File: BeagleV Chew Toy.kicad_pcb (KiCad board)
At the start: 2 copper layers, 69.2 x 51.7 mm, 147 parts, among them J1 Conn_02x05_Counter_Clockwise, J2 Conn_02x05_Counter_Clockwise, J3 Conn_02x05_Counter_Clockwise, U1 74HC245, U2 74HC245, U3 74HC245, U4 74HC245

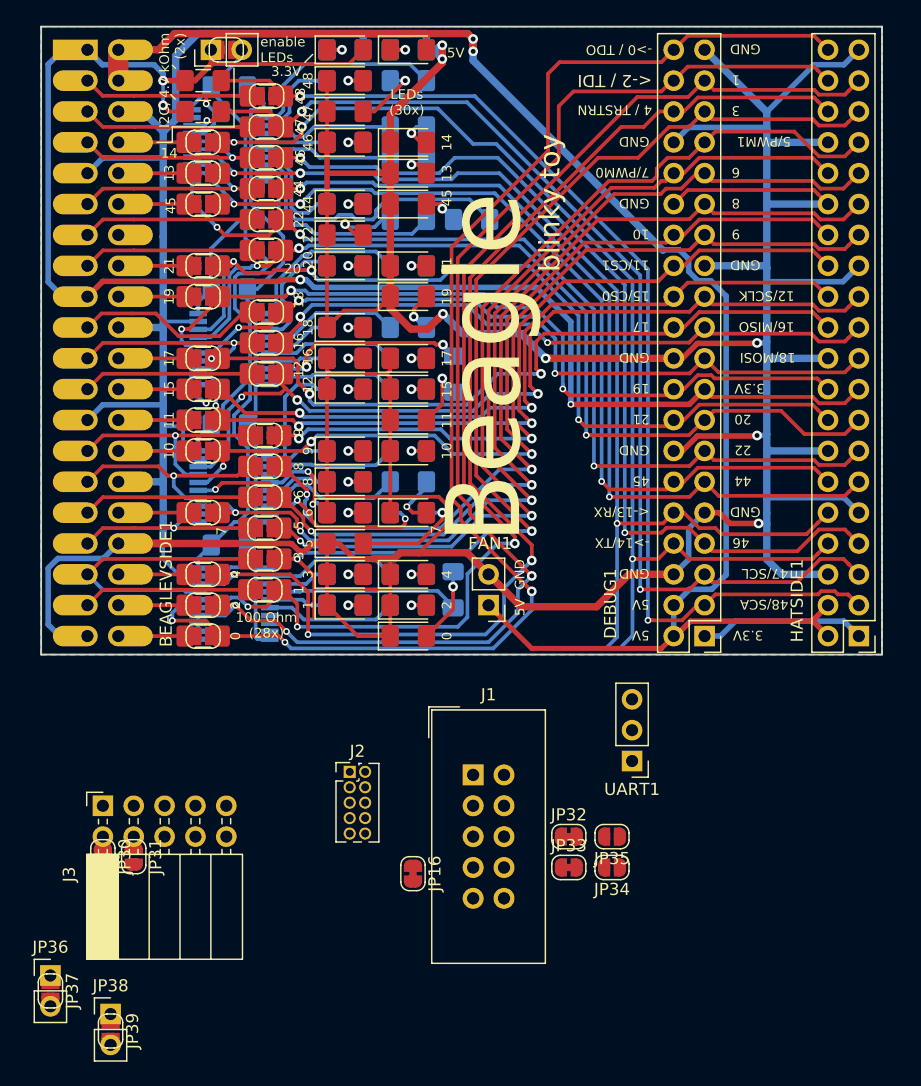
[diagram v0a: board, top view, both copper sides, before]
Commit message: small silk improvements
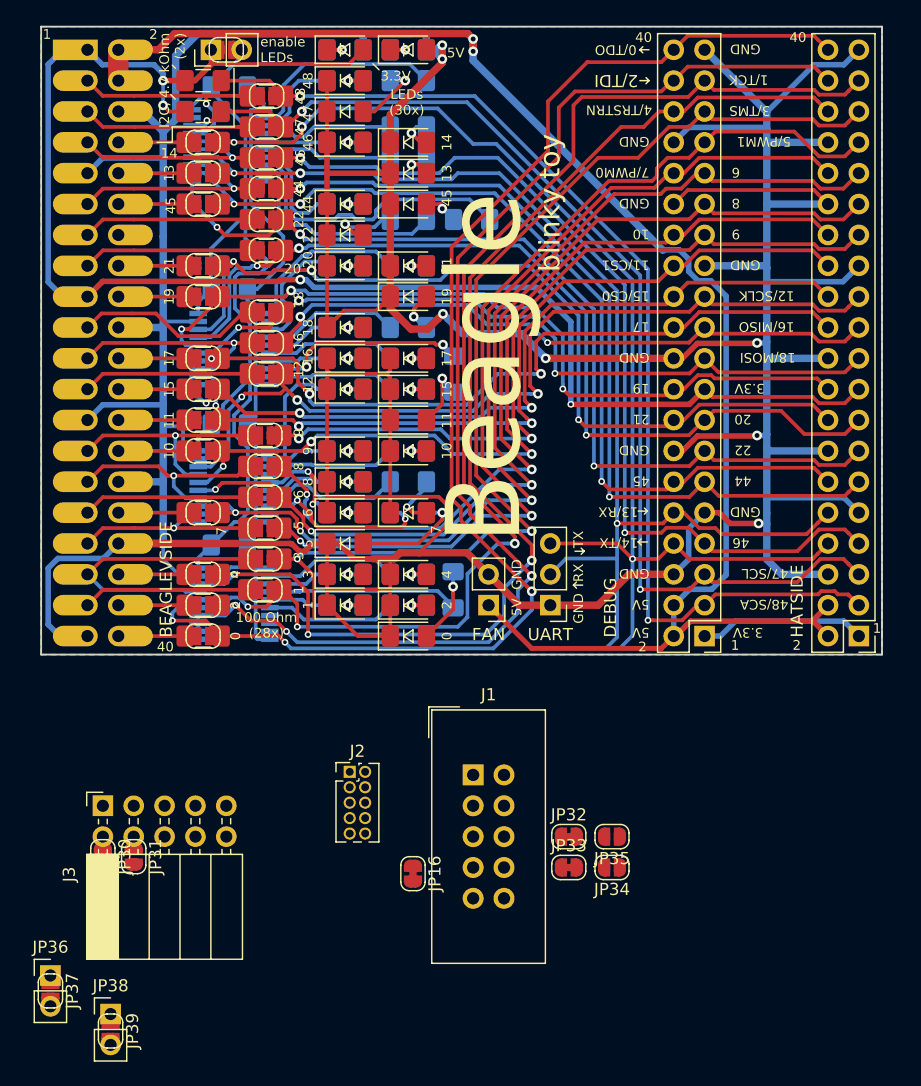
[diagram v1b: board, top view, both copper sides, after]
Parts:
- C1, C2, C3, C4: value 100n -> 100nF
- moved UART1 14.5 mm to (167.8, 126.5)
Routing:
- net /GPIO14/TX: track 94.0 -> 101.2 mm
- net /GPIO13/RX: track 90.9 -> 96.9 mm
- net /GPIO1_TCK: track 99.2 -> 101.9 mm
- net /GPIO0_TDO_FROM_SOC: track 110.9 -> 109.5 mm
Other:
- board text added: "0/TDO"
- board text added: "1/TCK"
- board text added: "13/RX"
- board text added: "14/TX"
- board text added: "2/TDI"
- board text added: "3/TMS"
- board text added: "4/TRSTRN"
- board text added: "40"
- board text added: "BEAGLEVSIDE"
- board text added: "DEBUG"
- board text added: "FAN"
- board text added: "HATSIDE"
- board text added: "RX"
- board text added: "TX"
- board text added: "UART"
- board text removed: "- connect UART - make 5V, 3V3, GND wider - add silk for LEDs"
- board text removed: "->0 / TDO"
- board text removed: "->14/TX"
- board text removed: "4 / TRSTRN"
- board text removed: "<-13/RX"
- board text removed: "<-2 / TDI"

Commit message: mostly done
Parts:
- added G***: LOGO, BeagleV Chew Toy:subraum_5mm, B.Cu at (165.5, 83.4)
- added G***: LOGO, BeagleV Chew Toy:subraum_5mm, F.Cu at (169.2, 116.6)
- added G***: LOGO, BeagleV Chew Toy:subraum_5mm, F.Cu at (190.4, 136.1)
- added G***: LOGO, BeagleV Chew Toy:subraum_10mm, B.Cu at (189.2, 134.9)
- JP32, JP33, JP34, JP35: moved to B.Cu
- moved JP37 60.8 mm to (183.0, 135.4), turned to 90 degrees
- moved JP36 59.9 mm to (183.0, 136.7), turned to 180 degrees
- moved JP39 53.2 mm to (177.9, 135.4), turned to 90 degrees
- moved JP38 52.0 mm to (177.9, 136.7), turned to 180 degrees
- moved JP31 43.1 mm to (173.2, 130.6), turned to 90 degrees
- moved JP30 42.7 mm to (170.3, 130.6), turned to 90 degrees
- moved JP34 33.2 mm to (144.0, 131.7), turned to 90 degrees
- moved J3 33.0 mm to (162.7, 134.1)
- moved JP33 32.4 mm to (141.4, 131.7), turned to 90 degrees
- moved J1 29.6 mm to (132.1, 136.7), turned to 90 degrees
- moved JP35 27.3 mm to (149.4, 131.7), turned to 90 degrees
- moved JP32 26.5 mm to (146.7, 131.7), turned to 90 degrees
- moved JP16 13.6 mm to (149.0, 137.3)
- moved J2 4.33 mm to (151.5, 135.9), turned to 90 degrees
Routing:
- net +3V3: track 143.3 -> 244.5 mm, vias 4 -> 5
- net GND: track 557.4 -> 607.6 mm, vias 7 -> 9
- net /GPIO3_TMS: track 88.5 -> 131.4 mm, vias 2 -> 4
- net /GPIO4_TRSTN: track 99.1 -> 138.5 mm, vias 3 -> 4
- net /GPIO1_TCK: track 101.9 -> 136.6 mm, vias 3 -> 5
- net Net-(J1-Pad8): track 0.00 -> 22.8 mm, vias 0 -> 2
- net Net-(J1-Pad6): track 0.00 -> 20.4 mm, vias 0 -> 3
- net Net-(J1-Pad7): track 0.00 -> 17.9 mm
- net Net-(J1-Pad9): track 0.00 -> 16.7 mm
- net Net-(J3-Pad6): track 0.00 -> 16.2 mm
- net /GPIO2_TDI_TO_SOC: track 105.0 -> 118.6 mm, vias 3 -> 4
- net Net-(J3-Pad2): track 0.00 -> 12.3 mm, vias 0 -> 2
- net Net-(J3-Pad4): track 0.00 -> 11.6 mm, vias 0 -> 1
- net /GPIO14/TX: track 101.2 -> 109.9 mm
- net Net-(J3-Pad8): track 0.00 -> 8.58 mm
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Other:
- board size 69.2 x 51.7 mm -> 69.2 x 61.6 mm
- board text added: "ARM 10-pin"
- board text added: "BEAGLEV SIDE"
- board text added: "GNDDetect"
- board text added: "HAT SIDE"
- board text added: "Sipeed RV"
- board text added: "TCK"
- board text added: "TDO"
- board text added: "TMS"
- board text added: "TRST"
- board text removed: "BEAGLEVSIDE"
- board text removed: "HATSIDE"

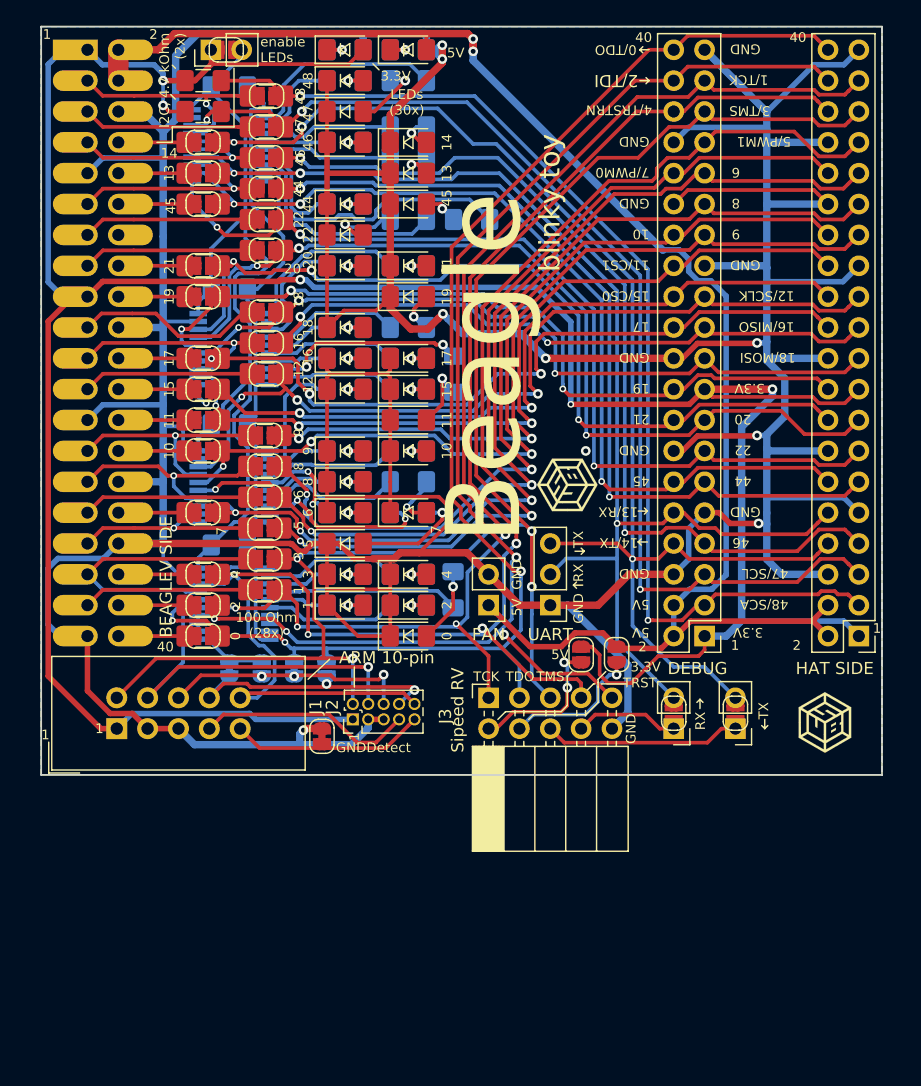
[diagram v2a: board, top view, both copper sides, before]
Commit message: rotate text in silk
Some of it was in a different orientation than the others.
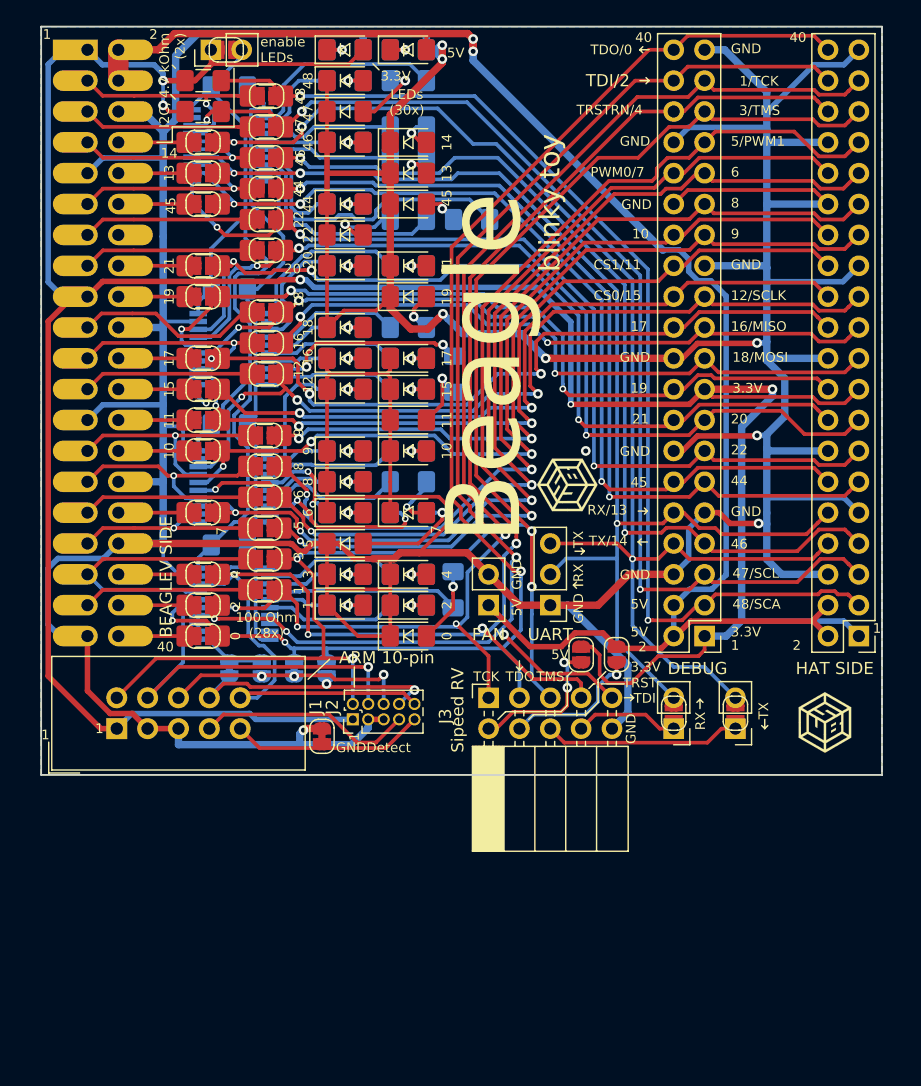
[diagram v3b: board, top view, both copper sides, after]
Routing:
- net GND: track 607.6 -> 609.4 mm
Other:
- board text added: "CS0/15"
- board text added: "CS1/11"
- board text added: "PWM0/7"
- board text added: "RX/13"
- board text added: "TDI"
- board text added: "TDI/2"
- board text added: "TDI/TDO flipped"
- board text added: "TDO/0"
- board text added: "TRSTRN/4"
- board text added: "TX/14"
- board text removed: "0/TDO"
- board text removed: "11/CS1"
- board text removed: "13/RX"
- board text removed: "14/TX"
- board text removed: "15/CS0"
- board text removed: "2/TDI"
- board text removed: "4/TRSTRN"
- board text removed: "7/PWM0"

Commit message: bugfix: lower left corner would have collided with heatsink mount
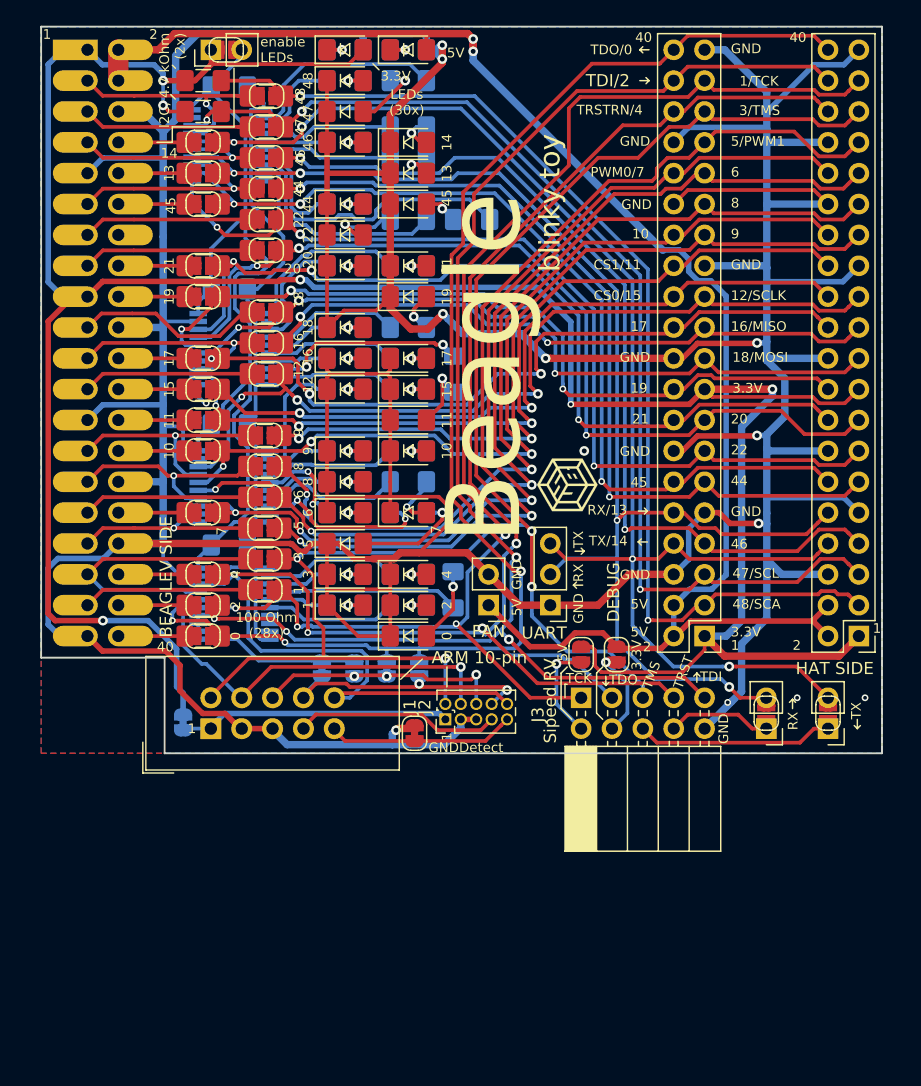
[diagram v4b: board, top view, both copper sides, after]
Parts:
- removed the G*** at (189.2, 134.9)
- added JP42: SolderJumper_2_Bridged, Jumper:SolderJumper-2_P1.3mm_Bridged_RoundedPad1.0x1.5mm, B.Cu at (137.5, 136.1)
- G***: moved to B.Cu
- moved G*** 20.4 mm to (185.7, 116.3), turned to 180 degrees
- moved J1 7.75 mm to (139.8, 136.7)
- moved JP16 7.62 mm to (156.6, 137.0)
- moved J2 7.62 mm to (159.1, 135.9)
- moved JP32 7.62 mm to (154.3, 131.7)
- moved JP33 7.62 mm to (149.0, 131.7)
- moved JP34 7.62 mm to (151.6, 131.7)
- moved JP35 7.62 mm to (157.0, 131.7)
- moved JP36 7.62 mm to (190.6, 136.7)
- moved JP37 7.62 mm to (190.6, 135.4)
- moved JP38 7.62 mm to (185.5, 136.7)
- moved JP39 7.62 mm to (185.5, 135.4)
- moved J3 7.62 mm to (170.3, 134.1)
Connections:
- J1 pad 1: +3V3 -> Net-(J1-Pad1)
- J2 pad 1: +3V3 -> Net-(J1-Pad1)
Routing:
- net Net-(J1-Pad1): track 0.00 -> 22.5 mm
- net /GPIO2_TDI_TO_SOC: track 118.6 -> 136.1 mm
- net /GPIO4_TRSTN: track 138.5 -> 153.1 mm
- net +3V3: track 244.5 -> 232.1 mm, vias 5 -> 6
- net /GPIO1_TCK: track 136.6 -> 146.0 mm
- net /GPIO0_TDO_FROM_SOC: track 113.9 -> 122.6 mm
- net /GPIO14/TX: track 109.9 -> 117.5 mm, vias 3 -> 4
- net /GPIO13/RX: track 102.5 -> 110.0 mm, vias 3 -> 4
- net GND: track 609.4 -> 616.7 mm, vias 9 -> 12
- net /GPIO3_TMS: track 131.4 -> 136.5 mm
- net Net-(J3-Pad2): track 12.3 -> 8.25 mm, vias 2 -> 1
- net Net-(J3-Pad4): track 11.6 -> 7.62 mm
- net Net-(J1-Pad9): track 16.7 -> 15.8 mm
- net Net-(J1-Pad7): track 17.9 -> 17.0 mm
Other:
- board size 69.2 x 61.6 mm -> 69.2 x 59.8 mm

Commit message: add UART1 and PWM2 to silk screen
also add the .sch file again...
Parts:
- moved G*** 3.06 mm to (169.4, 113.5)
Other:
- board text added: "I2C1"
- board text added: "PWM2/45"
- board text added: "UART1 9/RX"
- board text added: "UART1 TX/10"
- board text added: "UART3"
- board text removed: "UART"
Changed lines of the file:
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@@
   (general
     (thickness 1.6)
-    (drawings 314)
+    (drawings 322)
     (tracks 1793)
     (zones 0)
@@
   )
   (module "BeagleV Chew Toy:subraum_5mm" (layer Top)
-    (at 169.164 116.586 90)
+    (at 169.418 113.538 90)
     (fp_text reference G*** (at 0 0 90) (layer F.SilkS) hide
       (effects (font (size 1.524 1.524) (thickness 0.3)))
@@
     )
   )
+  (gr_line (start 175.133 96.012) (end 175.387 96.266) (layer F.SilkS) (width 0.12))
+  (gr_line (start 175.895 96.012) (end 175.133 96.012) (layer F.SilkS) (width 0.12))
+  (gr_line (start 175.133 96.012) (end 175.387 95.758) (layer F.SilkS) (width 0.12))
+  (gr_line (start 183.261 96.139) (end 182.499 96.139) (layer F.SilkS) (width 0.12))
+  (gr_line (start 182.499 96.139) (end 182.753 96.393) (layer F.SilkS) (width 0.12))
+  (gr_line (start 182.499 96.139) (end 182.753 95.885) (layer F.SilkS) (width 0.12))
+  (gr_text UART3 (at 170.815 120.523) (layer F.SilkS)
+    (effects (font (size 0.8 0.8) (thickness 0.1)) (justify left bottom))
+  )
+  (gr_text I2C1 (at 184.658 125.476) (layer F.SilkS)
+    (effects (font (size 0.8 0.8) (thickness 0.1)) (justify left bottom))
+  )
   (gr_text 3.3V (at 138.811 133.985) (layer B.SilkS)
     (effects (font (size 0.8 0.8) (thickness 0.1)) (justify left mirror))
@@
     (effects (font (size 0.8 0.8) (thickness 0.1)) (justify left bottom))
   )
-  (gr_text UART (at 167.259 128.778) (layer F.SilkS)
+  (gr_text UART3 (at 167.259 128.778) (layer F.SilkS)
     (effects (font (size 1 1) (thickness 0.15)))
   )
@@
     (effects (font (size 0.8 0.8) (thickness 0.1)) (justify left bottom))
   )
-  (gr_text 9 (at 182.626 96.393) (layer F.SilkS)
+  (gr_text "UART1\n9/RX" (at 183.261 97.282) (layer F.SilkS)
     (effects (font (size 0.8 0.8) (thickness 0.1)) (justify left bottom))
   )
@@
     (effects (font (size 0.8 0.8) (thickness 0.1)) (justify left bottom))
   )
-  (gr_text 45 (at 174.371 116.84) (layer F.SilkS)
-    (effects (font (size 0.8 0.8) (thickness 0.1)) (justify left bottom))
+  (gr_text PWM2/45 (at 176.149 116.713) (layer F.SilkS)
+    (effects (font (size 0.8 0.8) (thickness 0.1)) (justify right bottom))
   )
   (gr_text GND (at 173.482 114.3) (layer F.SilkS)
@@
     (effects (font (size 0.8 0.8) (thickness 0.1)) (justify left bottom))
   )
-  (gr_text 10 (at 174.498 96.393) (layer F.SilkS)
-    (effects (font (size 0.8 0.8) (thickness 0.1)) (justify left bottom))
+  (gr_text "UART1\nTX/10" (at 175.133 97.028) (layer F.SilkS)
+    (effects (font (size 0.8 0.8) (thickness 0.1)) (justify right bottom))
   )
   (gr_text GND (at 173.609 93.98) (layer F.SilkS)

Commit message: add wire colors to UART connector
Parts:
- moved G*** 5.86 mm to (171.2, 108.0)
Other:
- board text added: "white green black"
